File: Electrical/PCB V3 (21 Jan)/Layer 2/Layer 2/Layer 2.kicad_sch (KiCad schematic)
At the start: 90 parts, among them J1 XT60-M, Q1 AON6354, Q2 AON6354, Q3 AON6354, Q4 AON6354, SW1 SW_Nidec_CAS-120A1, U1 TPS5430DDA, U2 TPS5430DDA, U3 VNH5019ATR-E, U4 XT30UPB-M, U5 XT30UPB-M, U6 VNH5019ATR-E, U7 VNH5019ATR-E, U8 VNH5019ATR-E

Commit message: new bucky
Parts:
- removed C12: 10u, footprints:cap0603, symbol Device:C
- removed C13: 10n, footprints:cap0603, symbol Device:C
- removed C14: 220u, footprints:EIA-7343-D, symbol Device:C_Polarized
- removed C5, C7: 470u, Sen Robo:CP_Radial_D8.0mm_P3.50mm, symbol Device:C_Polarized
- removed J1: XT60-M, layer2v3:AMASS_XT60-M, symbol XT60-M:XT60-M
- removed L2: 15uH, footprints:0630 One Piece Inductor, symbol Device:L_Iron
- removed R36: 10K, footprints:res0603, symbol Device:R
- removed R37: 3K24, footprints:res0603, symbol Device:R
- removed U2: TPS5430DDA, footprints:TI_SO-PowerPAD-8_ThermalVias, symbol Regulator_Switching:TPS5430DDA
- added L2: L, symbol Device:L
- added U2: LM2596S-3.3, Package_TO_SOT_SMD:TO-263-5_TabPin3, symbol Regulator_Switching:LM2596S-3.3
- added U9: XT30UPB-M, layer2v3:AMASS_XT60-M, symbol amass xt 30:XT30UPB-M
- C1, C3: value 470u -> 220u; footprint Sen Robo:CP_Radial_D8.0mm_P3.50mm -> footprints:EIA-7343-D; LCSC C5162352 -> (none)
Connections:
- net +12V: now also C1.1, U2.1 (VIN), U9.P$2 (-)
- net +3V3: now also C3.1, L2.2, U2.4 (FB)
- net GND: now also U2.3 (GND), U2.5 (~{ON}/OFF), U9.P$1 (+)
- net Motor 2 EN A: now also R15.1; no longer R13.1
- net Motor 2 EN B: now also R16.1; no longer R14.1
- net Motor 3 EN A: now also R23.1; no longer R21.1
- net Motor 3 EN B: now also R24.1; no longer R22.1
- net Motor 4 EN A: now also R31.1; no longer R26.1, R29.1
- net Motor 4 EN B: now also R26.1, R32.1; no longer R30.1
- net Motor Driver: now also R13.1, R14.1, R21.1, R22.1, R29.1, R30.1; no longer R15.1, R16.1, R23.1, R24.1, R31.1, R32.1
- net at D2.1 (K): now also L2.1, U2.2 (OUT)
- net at C4.1, Q2.5 (D), Q2.6 (D)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: no longer C3.1
- net at C2.1, Q1.5 (D), Q1.6 (D)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: no longer C1.1
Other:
- moved on the sheet: C11, C2, C4, C6, C8, D1, R35

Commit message: 3 frivers add
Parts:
- removed H17, H18, H19, H20: MountingHole, MountingHole:MountingHole_3.2mm_M3_DIN965_Pad, symbol Mechanical:MountingHole

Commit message: 2 motor controller
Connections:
- net 12V is gone; now on net +12V: Q1.1 (S), Q1.2 (S), Q1.3 (S), Q2.1 (S), Q2.2 (S), Q2.3 (S), Q3.1 (S), Q3.2 (S), Q3.3 (S), Q4.1 (S), Q4.2 (S), Q4.3 (S), U3.12 (VBAT), U6.12 (VBAT), U7.12 (VBAT), U8.12 (VBAT)
- net Motor 1 Out B is gone; now on net Motor 2 Out B: U3.15 (OUTB), U3.16 (OUTB), U3.21 (OUTB), U3.HS3 (OUTB)
- net Motor 2 Out B: no longer U6.15 (OUTB), U6.16 (OUTB), U6.21 (OUTB), U6.HS3 (OUTB)
- net Motor 4 Out A renamed Motor 4 Motor B
- new net Motor 2 BOut : U6.15 (OUTB), U6.16 (OUTB), U6.21 (OUTB), U6.HS3 (OUTB)

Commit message: halfway done with motor drivers footprint vias are gay
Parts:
- added U10: Pinhead1, Connector_PinHeader_2.54mm:PinHeader_1x02_P2.54mm_Vertical_SMD_Pin1Right, symbol amass xt 30:XT30UPB-M
- added U11: Pinhead 2, Connector_PinHeader_2.54mm:PinHeader_1x02_P2.54mm_Vertical_SMD_Pin1Right, symbol amass xt 30:XT30UPB-M
- L2: footprint (none) -> Connector_PinHeader_2.54mm:PinHeader_1x02_P2.54mm_Vertical_SMD_Pin1Right
- U3, U6, U7, U8: footprint layer2v3:IC_VNH5019ATR-E -> layer2v3:fixed -onenew
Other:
- moved on the sheet: U9

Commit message: yay fixed motor driver do rest mr cos tired djbfj
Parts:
- U3, U6, U7, U8: footprint layer2v3:fixed -onenew -> layer2v3:fixed -onenew-newer
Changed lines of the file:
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@@
 			)
 		)
-		(property "Footprint" "layer2v3:fixed -onenew"
+		(property "Footprint" "layer2v3:fixed -onenew-newer"
 			(at 351.79 152.4 0)
 			(effects
@@
 			)
 		)
-		(property "Footprint" "layer2v3:fixed -onenew"
+		(property "Footprint" "layer2v3:fixed -onenew-newer"
 			(at 158.75 152.4 0)
 			(effects
@@
 			)
 		)
-		(property "Footprint" "layer2v3:fixed -onenew"
+		(property "Footprint" "layer2v3:fixed -onenew-newer"
 			(at 62.23 152.4 0)
 			(effects
@@
 			)
 		)
-		(property "Footprint" "layer2v3:fixed -onenew"
+		(property "Footprint" "layer2v3:fixed -onenew-newer"
 			(at 255.27 152.4 0)
 			(effects

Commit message: cx is annoyingwith 1 drivers
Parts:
- removed U4, U5: XT30UPB-M, layer2v3:XT30UPB-M, symbol XT30UPB-M:XT30UPB-M
- added J1: Conn_01x04, Connector_JST:JST_EH_B4B-EH-A_1x04_P2.50mm_Vertical, symbol Connector_Generic:Conn_01x04
- added J2: Conn_01x06, Connector_JST:JST_EH_B6B-EH-A_1x06_P2.50mm_Vertical, symbol Connector_Generic:Conn_01x06
- added U4, U5: XT30UPB-M, layer2v3:XT30UPB-M, symbol amass xt 30:XT30UPB-M
- A1: footprint layer2v3:TEENSY_SHORT -> layer2v3:MODULE_DEV-15583
- U10: value Pinhead1 -> XT30UPB-M; footprint Connector_PinHeader_2.54mm:PinHeader_1x02_P2.54mm_Vertical_SMD_Pin1Right -> layer2v3:XT30UPB-M
- U11: value Pinhead 2 -> XT30UPB-M; footprint Connector_PinHeader_2.54mm:PinHeader_1x02_P2.54mm_Vertical_SMD_Pin1Right -> layer2v3:XT30UPB-M
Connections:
- net Motor 2 BOut  is gone; now on net Motor 2 Out B: U6.15 (OUTB), U6.16 (OUTB), U6.21 (OUTB), U6.HS3 (OUTB)
- net Motor 4 Motor B is gone; now on net Motor 4 Out A: U8.1 (OUTA), U8.25 (OUTA), U8.30 (OUTA), U8.HS2 (OUTA)
- net +3V3: now also J1.4 (Pin_4), J2.1 (Pin_1); no longer A1.3.3V_1, A1.3.3V_2
- net GND: now also J1.1 (Pin_1), J2.6 (Pin_6)
- net Motor 1 Out A: now also U4.P$1 (+)
- net Motor 2 Out A: now also U10.P$1 (+)
- net Motor 2 Out B: now also U10.P$2 (-); no longer U3.15 (OUTB), U3.16 (OUTB), U3.21 (OUTB), U3.HS3 (OUTB)
- net Motor 3 Out A: now also U5.P$1 (+)
- net Motor 3 Out B: now also U5.P$2 (-)
- net Motor 4 Out B: now also U11.P$2 (-)
- net Motor 4 Out A: now reaches U11.P$1 (+)
- new net L1 RX: J1.3 (Pin_3)
- new net L1 TX: J1.2 (Pin_2)
- new net L3 RX: J2.5 (Pin_5)
- new net L3 TX: J2.4 (Pin_4)
- new net Motor 1 Out B: U3.15 (OUTB), U3.16 (OUTB), U3.21 (OUTB), U3.HS3 (OUTB), U4.P$2 (-)
- new net SCL: J2.2 (Pin_2)
- new net SDA: J2.3 (Pin_3)
- no-connect marks 23 -> 25
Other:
- note added: "Batt"
- note added: "L1 JST"
- note added: "L3 JST"
- note added: "Motors :C"
- note removed: "Coonector thing"
- note removed: "Misc"

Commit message: last motor driver to be done and jst
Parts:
- removed J2: Conn_01x06, Connector_JST:JST_EH_B6B-EH-A_1x06_P2.50mm_Vertical, symbol Connector_Generic:Conn_01x06
- removed U9: XT30UPB-M, layer2v3:AMASS_XT60-M, symbol amass xt 30:XT30UPB-M
- added J2: Conn_02x04_Counter_Clockwise, Connector_JST:JST_PHD_B8B-PHDSS_2x04_P2.00mm_Vertical, symbol Connector_Generic:Conn_02x04_Counter_Clockwise
- added J3: XT60-M, layer2v3:AMASS_XT60-M, symbol XT60-M:XT60-M
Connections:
- net +12V: now also J3.N (NEG)
- net +3V3: now also J2.1 (Pin_1)
- net GND: now also J2.5 (Pin_5), J3.P (POS)
- net Motor 1 EN A: now also A1.12; no longer A1.13
- net Motor 1 EN B: now also A1.5; no longer A1.20
- net Motor 2 EN A: now also A1.6; no longer A1.19
- net Motor 2 EN B: now also A1.7; no longer A1.18
- net Motor 3 EN A: now also A1.8; no longer A1.17
- net Motor 3 EN B: now also A1.9; no longer A1.16
- net Motor 4 EN A: now also A1.10, R26.1; no longer A1.15
- net Motor 4 EN B: now also A1.11; no longer A1.14, R26.1
- net RX3: now reaches A1.21
- net RX3: now also J2.7 (Pin_7)
- new net RX1: A1.15, J2.2 (Pin_2)
- new net RX2: A1.16, J2.4 (Pin_4)
- new net TX1: A1.14, A1.20, J2.3 (Pin_3)
- new net TX2: A1.17, J2.8 (Pin_8)
- new net TX3: J2.6 (Pin_6)
- no-connect marks 25 -> 18
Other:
- note added: "Bost:C"

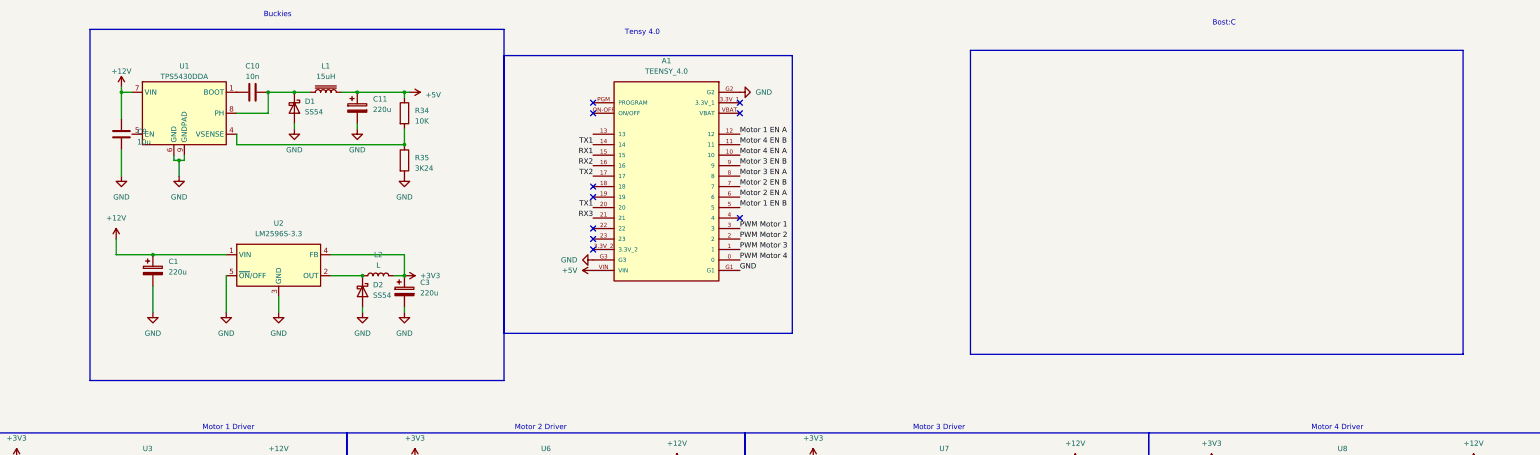
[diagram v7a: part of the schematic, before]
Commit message: motor drivers r done to be done tmr: diodes footbrint buckies boost capacitors and teensy pwm and motor feedback wiring
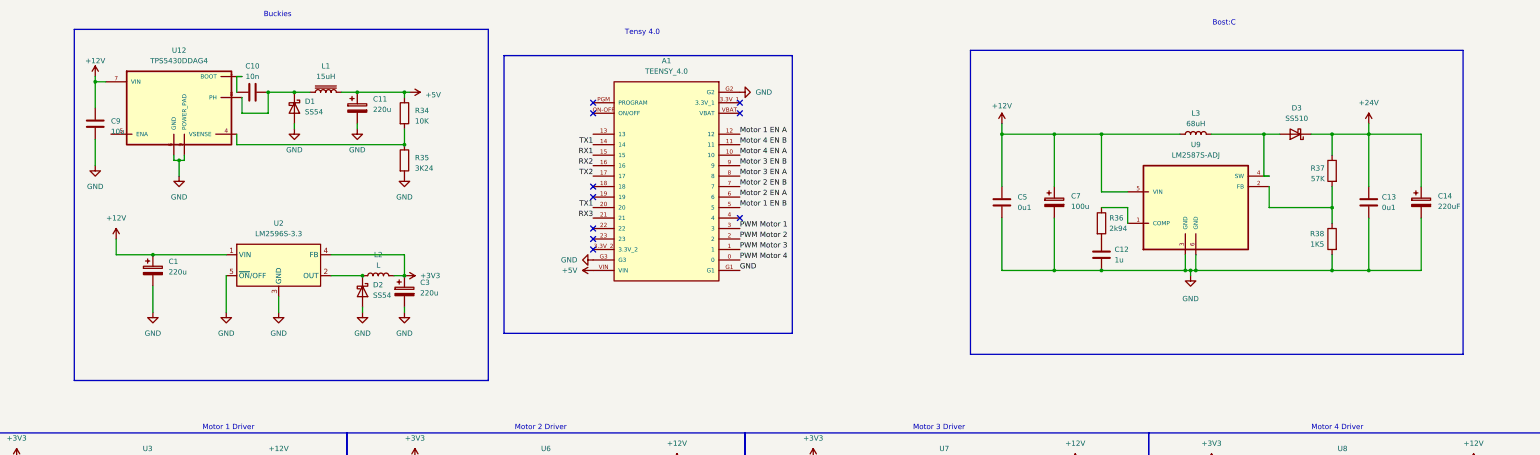
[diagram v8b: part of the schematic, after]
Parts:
- removed U1: TPS5430DDA, footprints:TI_SO-PowerPAD-8_ThermalVias, symbol Regulator_Switching:TPS5430DDA
- added C12: 1u, 2024l2:cap0603, symbol Device:C
- added C13, C5: 0u1, 2024l2:cap0603, symbol Device:C
- added C14: 220uF, Capacitor_SMD:CP_Elec_10x10.5, symbol Device:C_Polarized
- added C7: 100u, Capacitor_SMD:CP_Elec_8x6.5, symbol Device:C_Polarized
- added D3: SS510, 2024l2:SMA (DO-214AC), symbol Device:D_Schottky
- added L3: 68uH, Inductor_SMD:L_APV_APH1040, symbol Device:L
- added R36: 2k94, 2024l2:res0603, symbol Device:R
- added R37: 57K, 2024l2:res0603, symbol Device:R
- added R38: 1K5, 2024l2:res0603, symbol Device:R
- added U12: TPS5430DDAG4, layer2v3:VREG_TPS79625KTTR, symbol tps5430(buckie):TPS5430DDAG4
- added U9: LM2587S-ADJ, layer2v3:VREG_LM5017MR_NOPB, symbol lm2587(boost):LM2587S-ADJ
- L1: footprint footprints:0630 One Piece Inductor -> Inductor_SMD:L_0201_0603Metric
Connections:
- net +12V: now also C5.1, C7.1, L3.1, U12.7 (VIN), U9.5 (VIN)
- net GND: now also C12.2, C13.2, C14.2, C5.2, C7.2, R38.2, U12.6 (GND), U12.9 (POWER_PAD), U9.3 (GND), U9.6 (GND)
- net at C10.1: now also U12.1 (BOOT)
- net at C10.2, D1.1 (K), L1.1: now also U12.8 (PH)
- net at R34.2, R35.1: now also U12.4 (VSENSE)
- new net: R36.1, U9.1 (COMP)
- new net: R37.2, R38.1, U9.2 (FB)
- new net: D3.2 (A), L3.2, U9.4 (SW)
- new net: C12.1, R36.2
- new net +24V: C13.1, C14.1, D3.1 (K), R37.1
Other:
- moved on the sheet: C9
